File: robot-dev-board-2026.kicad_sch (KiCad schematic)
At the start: 25 parts, among them J1 USB_C_Receptacle_USB2.0_16P, J10 6V_Out_1, J11 6V_Out_2, J12 6V_Out_3, J13 6V_Out_4, J14 6V_Out_5, J15 6V_Out_6, J2 Out_1, J3 Out_2, J4 Out_3, J5 Out_4, J6 Out_5, J7 Out_6, J8 Out_7, J9 Out_8, SW1 SW_Nidec_CAS-120A1, U1 RP2040, U2 AMS1117-3.3, U3 LM7806_TO220

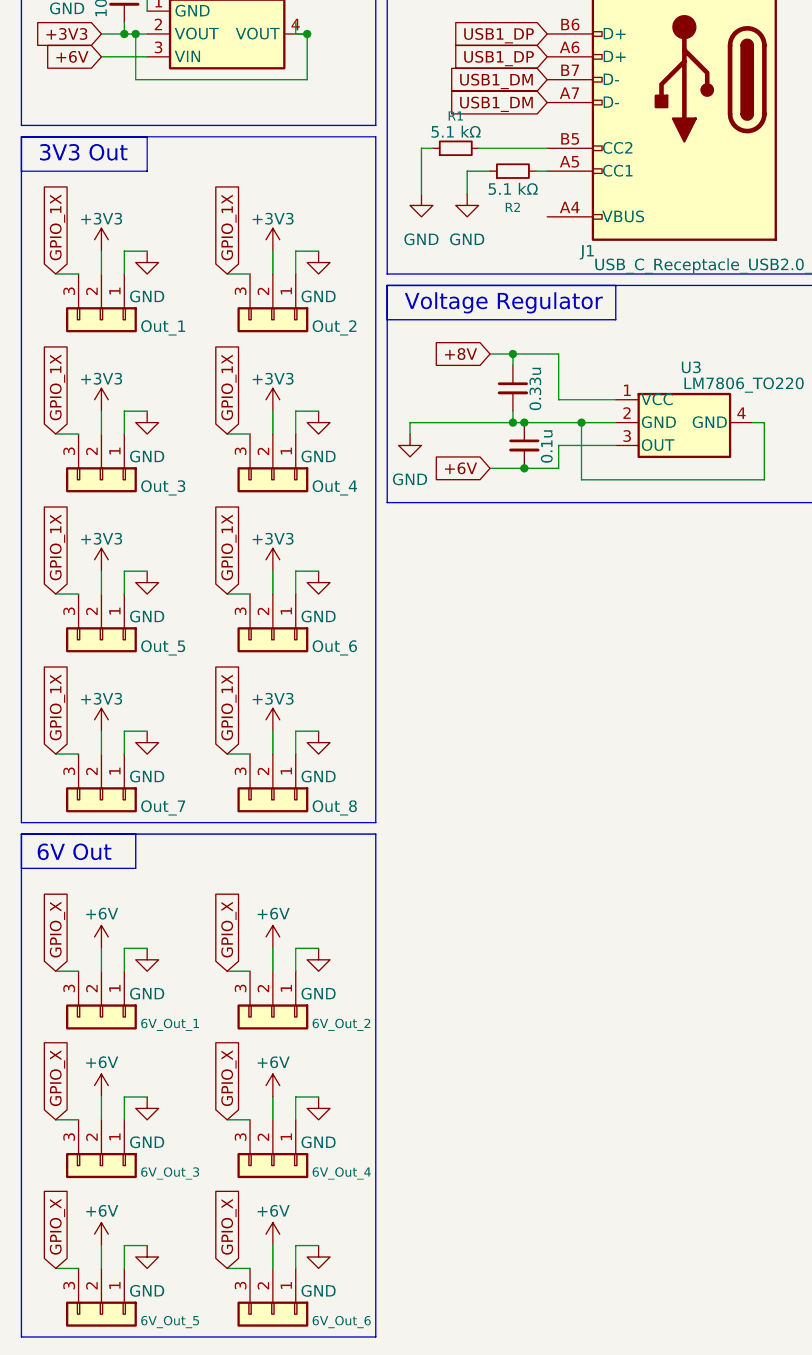
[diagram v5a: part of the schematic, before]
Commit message: Fixed net labels for 3V3 and 6V rails, added UART box
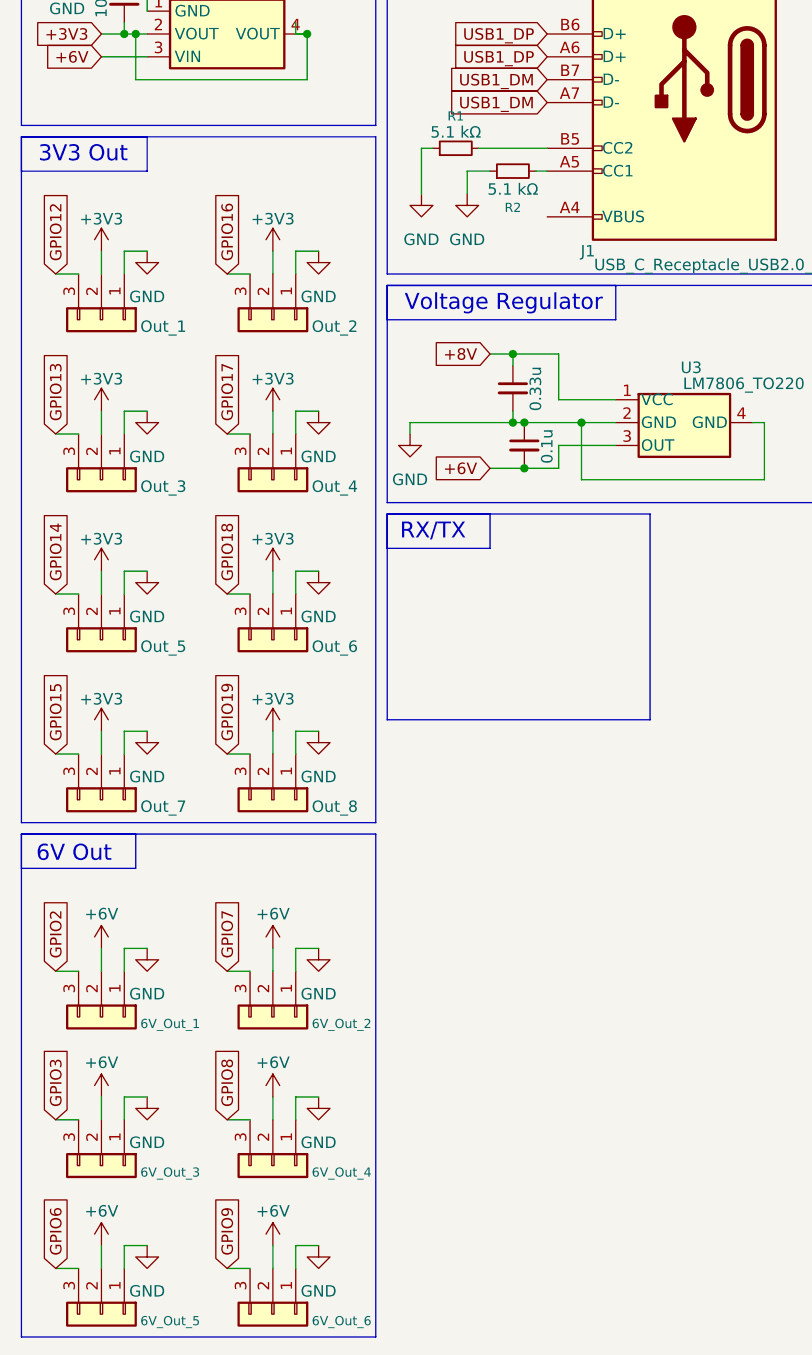
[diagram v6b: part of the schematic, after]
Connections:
- net GPIO12: now also J2.3 (Pin_3)
- net GPIO13: now also J4.3 (Pin_3)
- net GPIO14: now also J6.3 (Pin_3)
- net GPIO15: now also J8.3 (Pin_3)
- net GPIO16: now also J3.3 (Pin_3)
- net GPIO17: now also J5.3 (Pin_3)
- net GPIO18: now also J7.3 (Pin_3)
- net GPIO19: now also J9.3 (Pin_3)
- net GPIO2: now also J10.3 (Pin_3)
- net GPIO3: now also J12.3 (Pin_3)
- net GPIO6: now also J14.3 (Pin_3)
- net GPIO7: now also J11.3 (Pin_3)
- net GPIO8: now also J13.3 (Pin_3)
- net GPIO9: now also J15.3 (Pin_3)
- removed net GPIO_1X: J2.3 (Pin_3), J3.3 (Pin_3), J4.3 (Pin_3), J5.3 (Pin_3), J6.3 (Pin_3), J7.3 (Pin_3), J8.3 (Pin_3), J9.3 (Pin_3)
- removed net GPIO_X: J10.3 (Pin_3), J11.3 (Pin_3), J12.3 (Pin_3), J13.3 (Pin_3), J14.3 (Pin_3), J15.3 (Pin_3)
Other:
- note added: "RX/TX"
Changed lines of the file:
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@@
+	)
+	(rectangle
+		(start 54.61 86.36)
+		(end 83.82 109.22)
+		(stroke
+			(width 0)
+			(type default)
+		)
+		(fill
+			(type none)
+		)
 	)
 	(rectangle
@@
 	)
 	(rectangle
+		(start 54.61 86.36)
+		(end 66.04 90.17)
+		(stroke
+			(width 0)
+			(type default)
+		)
+		(fill
+			(type none)
+		)
+	)
+	(rectangle
 		(start 54.61 13.97)
 		(end 105.41 59.69)
@@
 		(exclude_from_sim no)
 		(at 19.812 124.206 0)
+		(effects
+			(font
+				(size 1.778 1.778)
+			)
+		)
+	)
+	(text "RX/TX"
+		(exclude_from_sim no)
+		(at 59.69 88.392 0)
 		(effects
 			(font
@@
 		)
 	)
-	(global_label "GPIO_X"
+	(global_label "GPIO2"
 		(shape input)
 		(at 17.78 137.16 90)
@@
 		)
 		(property "Intersheetrefs" "${INTERSHEET_REFS}"
-			(at 17.78 127.5224 90)
+			(at 17.78 128.49 90)
 			(effects
 				(font
@@
 		)
 	)
-	(global_label "GPIO_1X"
+	(global_label "GPIO18"
 		(shape input)
 		(at 36.83 95.25 90)
@@
 		)
 		(property "Intersheetrefs" "${INTERSHEET_REFS}"
-			(at 36.83 84.4029 90)
-			(effects
-				(font
-					(size 1.27 1.27)
-				)
-				(justify left)
-				(hide yes)
-			)
-		)
-	)
-	(global_label "GPIO_X"
+			(at 36.83 85.3705 90)
+			(effects
+				(font
+					(size 1.27 1.27)
+				)
+				(justify left)
+				(hide yes)
+			)
+		)
+	)
+	(global_label "GPIO3"
 		(shape input)
 		(at 17.78 153.67 90)
@@
 		)
 		(property "Intersheetrefs" "${INTERSHEET_REFS}"
-			(at 17.78 144.0324 90)
+			(at 17.78 145 90)
 			(effects
 				(font
@@
 		)
 	)
-	(global_label "GPIO_1X"
+	(global_label "GPIO12"
 		(shape input)
 		(at 17.78 59.69 90)
@@
 		)
 		(property "Intersheetrefs" "${INTERSHEET_REFS}"
-			(at 17.78 48.8429 90)
+			(at 17.78 49.8105 90)
 			(effects
 				(font
@@
 		)
 	)
-	(global_label "GPIO_X"
+	(global_label "GPIO8"
 		(shape input)
 		(at 36.83 153.67 90)
@@
 		)
 		(property "Intersheetrefs" "${INTERSHEET_REFS}"
-			(at 36.83 144.0324 90)
+			(at 36.83 145 90)
 			(effects
 				(font
@@
 		)
 	)
-	(global_label "GPIO_1X"
+	(global_label "GPIO13"
 		(shape input)
 		(at 17.78 77.47 90)
@@
 		)
 		(property "Intersheetrefs" "${INTERSHEET_REFS}"
-			(at 17.78 66.6229 90)
-			(effects
-				(font
-					(size 1.27 1.27)
-				)
-				(justify left)
-				(hide yes)
-			)
-		)
-	)
-	(global_label "GPIO_X"
+			(at 17.78 67.5905 90)
+			(effects
+				(font
+					(size 1.27 1.27)
+				)
+				(justify left)
+				(hide yes)
+			)
+		)
+	)
+	(global_label "GPIO6"
 		(shape input)
 		(at 17.78 170.18 90)
@@
 		)
 		(property "Intersheetrefs" "${INTERSHEET_REFS}"
-			(at 17.78 160.5424 90)
+			(at 17.78 161.51 90)
 			(effects
 				(font
@@
 		)
 	)
-	(global_label "GPIO_X"
+	(global_label "GPIO9"
 		(shape input)
 		(at 36.83 170.18 90)
@@
 		)
 		(property "Intersheetrefs" "${INTERSHEET_REFS}"
-			(at 36.83 160.5424 90)
+			(at 36.83 161.51 90)
 			(effects
 				(font
@@
 		)
 	)
-	(global_label "GPIO_1X"
+	(global_label "GPIO16"
 		(shape input)
 		(at 36.83 59.69 90)
@@
 		)
 		(property "Intersheetrefs" "${INTERSHEET_REFS}"
-			(at 36.83 48.8429 90)
+			(at 36.83 49.8105 90)
 			(effects
 				(font
@@
 		)
 	)
-	(global_label "GPIO_1X"
+	(global_label "GPIO19"
 		(shape input)
 		(at 36.83 113.03 90)
@@
 		)
 		(property "Intersheetrefs" "${INTERSHEET_REFS}"
-			(at 36.83 102.1829 90)
+			(at 36.83 103.1505 90)
 			(effects
 				(font
@@
 		)
 	)
-	(global_label "GPIO_X"
+	(global_label "GPIO7"
 		(shape input)
 		(at 36.83 137.16 90)
@@
 		)
 		(property "Intersheetrefs" "${INTERSHEET_REFS}"
-			(at 36.83 127.5224 90)
+			(at 36.83 128.49 90)
 			(effects
 				(font
@@
 		)
 	)
-	(global_label "GPIO_1X"
+	(global_label "GPIO14"
 		(shape input)
 		(at 17.78 95.25 90)
@@
 		)
 		(property "Intersheetrefs" "${INTERSHEET_REFS}"
-			(at 17.78 84.4029 90)
-			(effects
-				(font
-					(size 1.27 1.27)
-				)
-				(justify left)
-				(hide yes)
-			)
-		)
-	)
-	(global_label "GPIO_1X"
+			(at 17.78 85.3705 90)
+			(effects
+				(font
+					(size 1.27 1.27)
+				)
+				(justify left)
+				(hide yes)
+			)
+		)
+	)
+	(global_label "GPIO15"
 		(shape input)
 		(at 17.78 113.03 90)
@@
 		)
 		(property "Intersheetrefs" "${INTERSHEET_REFS}"
-			(at 17.78 102.1829 90)
+			(at 17.78 103.1505 90)
 			(effects
 				(font
@@
 		)
 	)
-	(global_label "GPIO_1X"
+	(global_label "GPIO17"
 		(shape input)
 		(at 36.83 77.47 90)
@@
 		)
 		(property "Intersheetrefs" "${INTERSHEET_REFS}"
-			(at 36.83 66.6229 90)
-			(effects
-				(font
+			(at 36.83 67.5905 90)
+			(effects
+				(font
